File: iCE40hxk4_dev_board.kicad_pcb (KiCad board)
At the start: 4 copper layers, 70 x 152 mm, 336 parts, among them J201 CONN_01X02, J202 USB_OTG, J401 CONN_01X20, J701 CONN_01X01, J702 CONN_01X01, U1001 ADC1175, U1002 ADC1175, U1101 MIC7300, U1102 MIC7300, U1103 MCP4716, U1104 MCP4716, U1105 MIC7300, U1106 MIC7300, U201 MIC2005A-2YM5, U203 93LCxxB_sot-23-6, U204 MIC5355/6-xYMME, U205 FT2232H, U301 iCE40-HX4K-TQ144, U302 25LC_EEPROM, U501 AS4C1M16S, U701 CPC1017N, U702 CPC1017N, U703 CD4051BM96, U704 CD4051BM96, U801 CD4051BM96, U802 CD4051BM96, U803 CLC4007, U901 LM2776DBVR, U902 TCR2EF13, U903 MIC5270

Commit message: Changed part number of DAC (different dir). Connected ADC_OE to GND.
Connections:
- J202 pad 4: (no net) -> Net-(J202-Pad4)
- U1001 pad 1: (no net) -> GND
- U1001 pad 16: (no net) -> Net-(U1001-Pad16)
- U1001 pad 22: (no net) -> Net-(U1001-Pad22)
- U1002 pad 1: (no net) -> GND
- U1002 pad 16: (no net) -> Net-(U1002-Pad16)
- U1002 pad 22: (no net) -> Net-(U1002-Pad22)
- U205 pad 19: (no net) -> Net-(U205-Pad19)
- U205 pad 22: (no net) -> Net-(U205-Pad22)
- U205 pad 29: (no net) -> Net-(U205-Pad29)
- U205 pad 3: (no net) -> Net-(U205-Pad3)
- U205 pad 30: (no net) -> Net-(U205-Pad30)
- U205 pad 32: (no net) -> Net-(U205-Pad32)
- U205 pad 33: (no net) -> Net-(U205-Pad33)
- U205 pad 34: (no net) -> Net-(U205-Pad34)
- U205 pad 36: (no net) -> Net-(U205-Pad36)
- U205 pad 57: (no net) -> Net-(U205-Pad57)
- U205 pad 58: (no net) -> Net-(U205-Pad58)
- U205 pad 59: (no net) -> Net-(U205-Pad59)
- U205 pad 60: (no net) -> Net-(U205-Pad60)
- U301 pad 109: (no net) -> Net-(U301-Pad109)
- U301 pad 133: (no net) -> Net-(U301-Pad133)
- U301 pad 35: (no net) -> Net-(U301-Pad35)
- U301 pad 36: (no net) -> Net-(U301-Pad36)
- U301 pad 50: (no net) -> Net-(U301-Pad50)
- U301 pad 51: (no net) -> Net-(U301-Pad51)
- U301 pad 58: (no net) -> Net-(U301-Pad58)
- U301 pad 77: (no net) -> Net-(U301-Pad77)
- U301 pad 91: (no net) -> /RIGHT_TOP_BANKs/IOT_139
- U501 pad 33: (no net) -> Net-(U501-Pad33)
- U501 pad 37: (no net) -> Net-(U501-Pad37)
- U902 pad 4: (no net) -> Net-(U902-Pad4)
- U903 pad 1: (no net) -> Net-(U903-Pad1)
- U903 pad 3: (no net) -> Net-(U903-Pad3)
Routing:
- net /RIGHT_TOP_BANKs/IOT_139: track 0.00 -> 107.8 mm
- net (no net): track 107.8 -> 0.00 mm

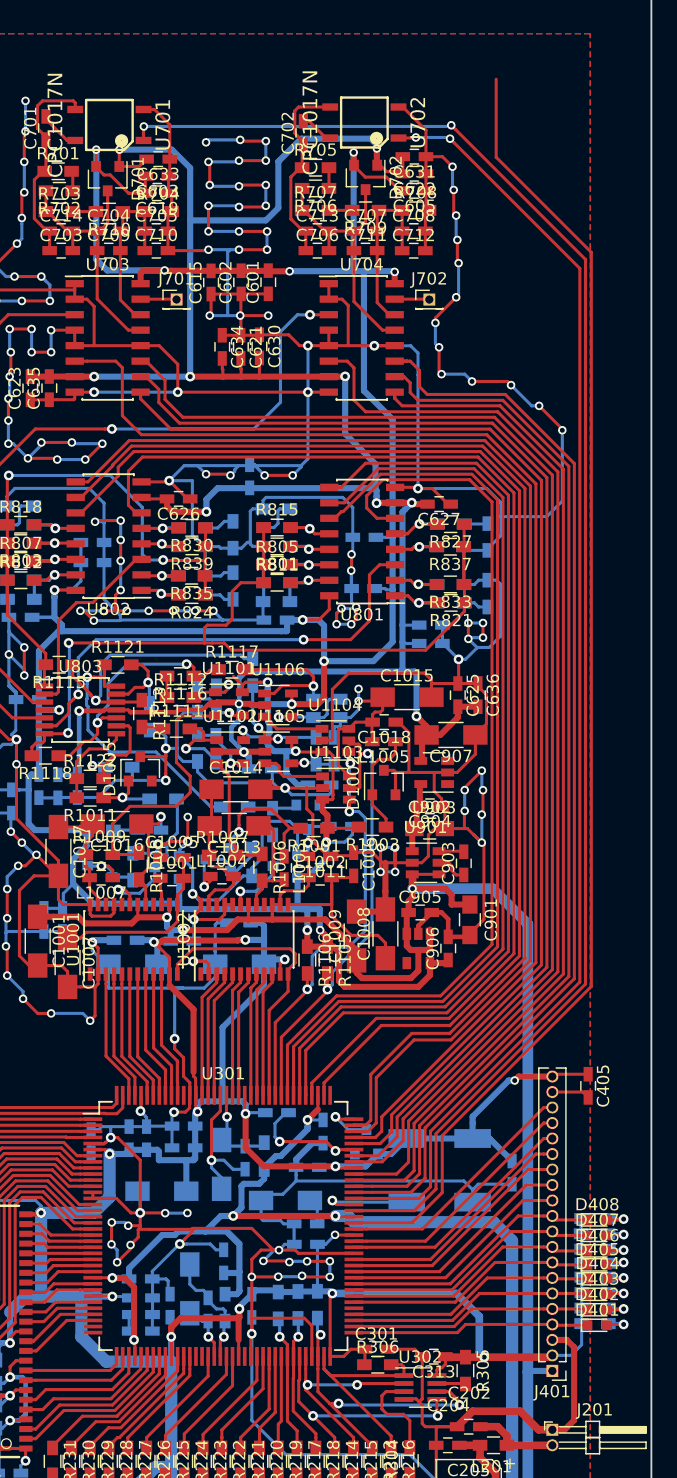
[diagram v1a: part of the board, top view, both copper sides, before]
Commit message: Added reset button. Delated unused fpga analog control connections. Added this connections to the expansion connector
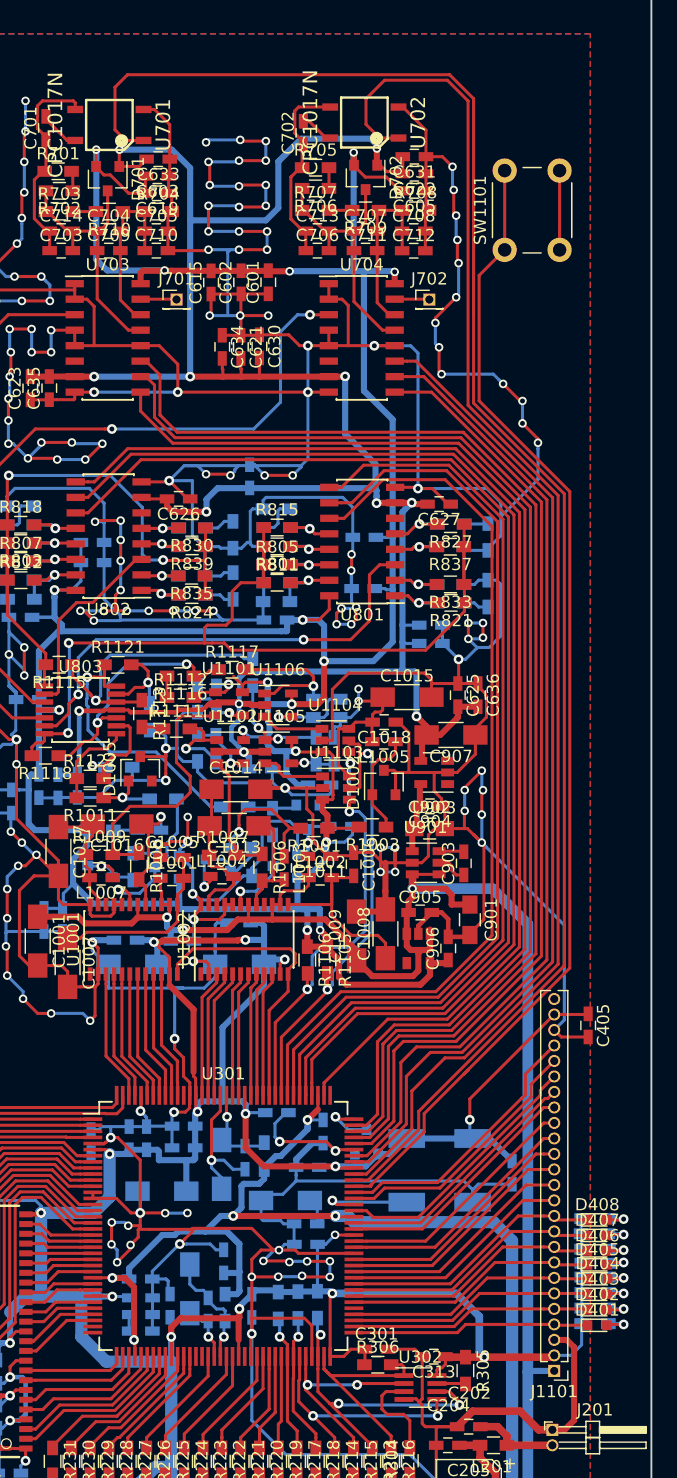
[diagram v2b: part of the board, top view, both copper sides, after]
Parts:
- removed J401: CONN_01X20, Pin_Headers:Pin_Header_Straight_1x20_Pitch1.27mm
- added J1101: CONN_01X25, Pin_Headers:Pin_Header_Straight_1x25_Pitch1.27mm, F.Cu at (146.0, 153.3)
- added SW1101: SW_Push, Buttons_Switches_THT:SW_PUSH_6mm_h4.3mm, F.Cu at (141.9, 61.4)
- moved C405 4.95 mm to (148.7, 125.0)
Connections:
- U301 pad 101: /Analog front end/CHA_ATT_SEL_0 -> /Analog front end/CHB_ATT_SEL_0
- U301 pad 102: /Analog front end/CHA_ATT_SEL_1 -> /Analog front end/CHB_ATT_SEL_1
- U301 pad 104: /Analog front end/CHA_ATT_SEL_2 -> /Analog front end/CHB_ATT_SEL_2
- U301 pad 105: /Analog front end/CHA_ATT_EN -> /Analog front end/CHA_ATT_SEL_0
- U301 pad 106: /Analog front end/CHB_GAIN_SEL_2 -> /Analog front end/CHA_ATT_SEL_1
- U301 pad 107: /Analog front end/CHB_GAIN_SEL_1 -> /Analog front end/CHA_ATT_SEL_2
- U301 pad 110: /Analog front end/CHB_GAIN_SEL_0 -> /Analog front end/CHB_GAIN_SEL_2
- U301 pad 112: /Analog front end/CHB_GAIN_EN -> /Analog front end/CHB_GAIN_SEL_1
- U301 pad 113: /Analog front end/CHA_GAIN_SEL_2 -> /Analog front end/CHB_GAIN_SEL_0
- U301 pad 114: /Analog front end/CHA_GAIN_SEL_1 -> /Analog front end/CHA_GAIN_SEL_2
- U301 pad 115: /Analog front end/CHA_GAIN_SEL_0 -> /Analog front end/CHA_GAIN_SEL_1
- U301 pad 116: /Analog front end/CHA_GAIN_EN -> /Analog front end/CHA_GAIN_SEL_0
- U301 pad 91: /RIGHT_TOP_BANKs/IOT_139 -> /RIGHT_TOP_BANKs/IOR_139
- U301 pad 93: /Analog front end/CHA_DC_COUPLING -> /RIGHT_TOP_BANKs/IOR_140
- U301 pad 95: /Analog front end/CHB_DC_COUPLING -> /RIGHT_TOP_BANKs/IOR_144
- U301 pad 96: /Analog front end/CHB_ATT_SEL_0 -> /RIGHT_TOP_BANKs/IOR_146
- U301 pad 97: /Analog front end/CHB_ATT_SEL_1 -> Net-(SW1101-Pad1)
- U301 pad 98: /Analog front end/CHB_ATT_SEL_2 -> /Analog front end/CHA_DC_COUPLING
- U301 pad 99: /Analog front end/CHB_ATT_EN -> /Analog front end/CHB_DC_COUPLING
- U703 pad 6: /Analog front end/CHA_ATT_EN -> GND
- U704 pad 6: /Analog front end/CHB_ATT_EN -> GND
- U801 pad 6: /Analog front end/CHA_GAIN_EN -> GND
- U802 pad 6: /Analog front end/CHB_GAIN_EN -> GND
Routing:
- net /RIGHT_TOP_BANKs/IOT_139: track 107.8 -> 0.00 mm
- net /Analog front end/CHA_ATT_EN: track 105.1 -> 0.00 mm
- net /Analog front end/CHB_GAIN_EN: track 97.2 -> 0.00 mm
- net Net-(SW1101-Pad1): track 0.00 -> 95.9 mm
- net /Analog front end/CHB_ATT_EN: track 90.6 -> 0.00 mm
- net /Analog front end/CHA_GAIN_EN: track 75.8 -> 0.00 mm
- net /Analog front end/CHA_DC_COUPLING: track 130.7 -> 154.3 mm, vias 2 -> 0
- net /RIGHT_TOP_BANKs/IOR_146: track 0.00 -> 22.4 mm
- net /RIGHT_TOP_BANKs/IOR_140: track 0.00 -> 21.9 mm
- net /RIGHT_TOP_BANKs/IOR_144: track 0.00 -> 21.7 mm
- net GND: track 1408.9 -> 1429.8 mm
- net /RIGHT_TOP_BANKs/IOR_139: track 0.00 -> 20.9 mm
- net /Analog front end/CHB_ATT_SEL_0: track 89.8 -> 81.0 mm
- net /Analog front end/CHB_DC_COUPLING: track 106.3 -> 114.4 mm, vias 2 -> 0
- net /Analog front end/CHB_ATT_SEL_1: track 87.1 -> 79.7 mm
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
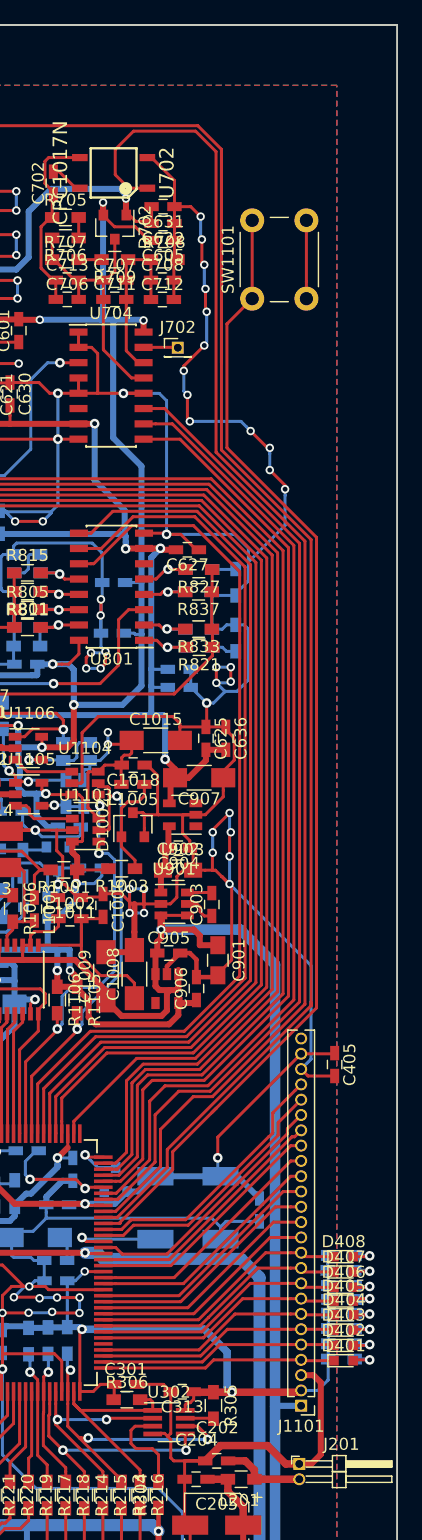
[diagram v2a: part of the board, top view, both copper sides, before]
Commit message: Added square wave output.
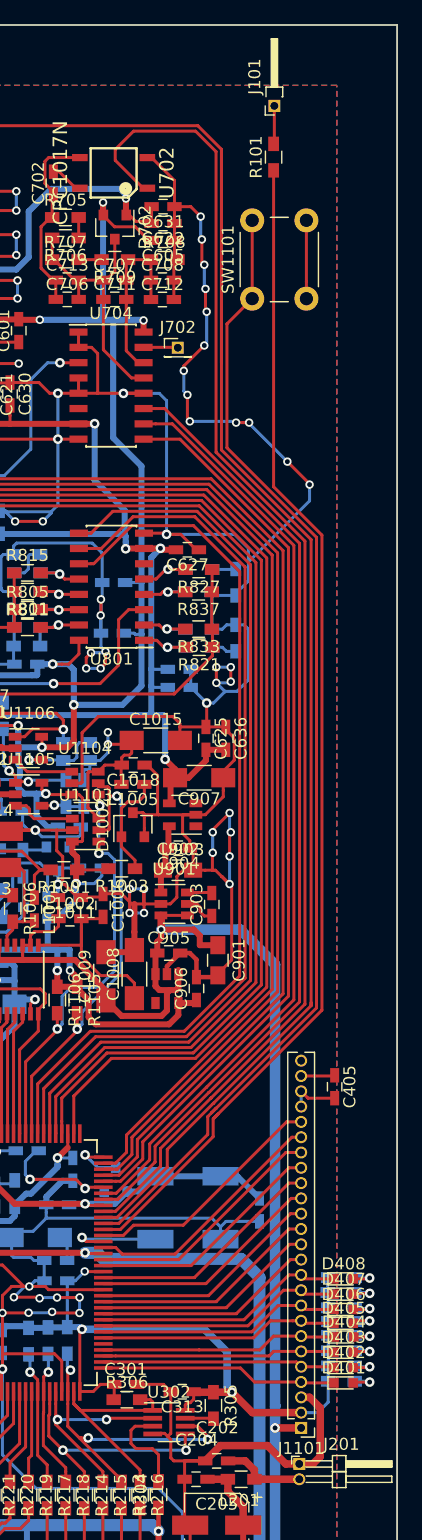
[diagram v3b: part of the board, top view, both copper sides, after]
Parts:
- added J101: CONN_01X01, Pin_Headers:Pin_Header_Angled_1x01_Pitch1.27mm, F.Cu at (143.7, 45.4)
- added R101: 10k, Resistors_SMD:R_0603_HandSoldering, F.Cu at (143.7, 49.7)
- moved D407 1.84 mm to (149.5, 144.1)
- moved R401 1.84 mm to (149.3, 151.3)
- moved C405 1.84 mm to (148.7, 126.8)
- moved D401 1.84 mm to (149.5, 151.4)
- moved D402 1.84 mm to (149.5, 150.2)
- moved D403 1.84 mm to (149.5, 148.9)
- moved D404 1.84 mm to (149.5, 147.6)
- moved D405 1.84 mm to (149.5, 146.5)
- moved D406 1.84 mm to (149.5, 145.3)
- moved D408 1.84 mm to (149.5, 142.8)
- moved J1101 1.84 mm to (146.0, 155.2)
- moved R402 1.84 mm to (149.3, 150.0)
- moved R403 1.84 mm to (149.3, 148.8)
- moved R404 1.84 mm to (149.3, 147.5)
- moved R405 1.84 mm to (149.3, 146.3)
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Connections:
- J1101 pad 22: /RIGHT_TOP_BANKs/IOR_146 -> GND
- U301 pad 96: /RIGHT_TOP_BANKs/IOR_146 -> /RIGHT_TOP_BANKs/IOT_146
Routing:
- net /RIGHT_TOP_BANKs/IOT_146: track 0.00 -> 98.3 mm
- net /RIGHT_TOP_BANKs/IOR_146: track 22.4 -> 0.00 mm
- net GND: track 1429.8 -> 1412.3 mm
- net +3V3: track 499.3 -> 487.3 mm, vias 29 -> 28
- net Net-(J101-Pad1): track 0.00 -> 3.18 mm
- net /Analog front end/CHA_ATT_SEL_2: track 95.9 -> 93.3 mm
- net /Analog front end/CHA_ATT_SEL_1: track 98.4 -> 95.8 mm
- net /Analog front end/CHA_ATT_SEL_0: track 100.6 -> 98.0 mm
- net /Analog front end/CHB_ATT_SEL_2: track 78.1 -> 75.5 mm
- net /Analog front end/CHB_ATT_SEL_1: track 79.7 -> 77.6 mm
- net /Analog front end/CHB_DC_COUPLING: track 114.4 -> 112.8 mm
- net /Analog front end/CHB_ATT_SEL_0: track 81.0 -> 79.5 mm
- net /RIGHT_TOP_BANKs/IOR_144: track 21.7 -> 20.3 mm
- net /Analog front end/CHB_GAIN_SEL_2: track 96.9 -> 98.2 mm
- net /RIGHT_TOP_BANKs/IOR_140: track 21.9 -> 20.9 mm
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
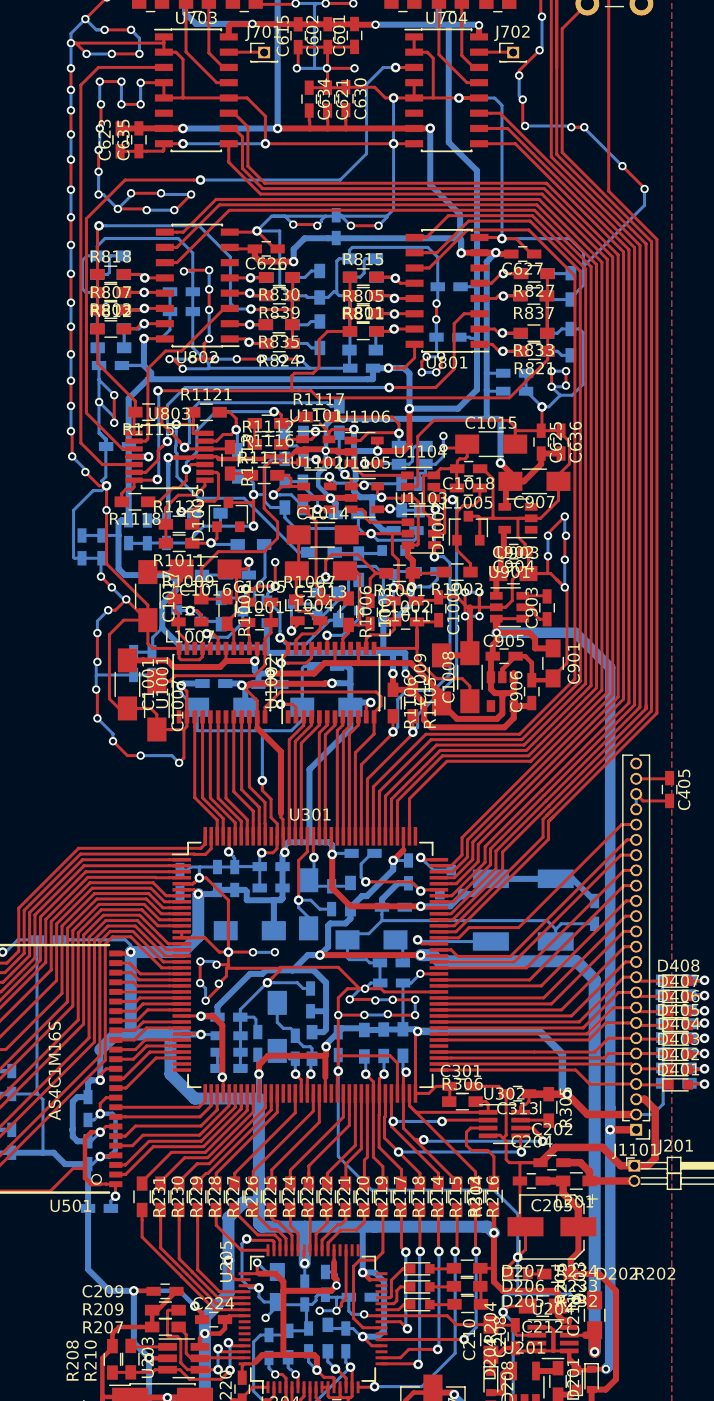
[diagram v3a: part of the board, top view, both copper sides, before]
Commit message: Moved some capacitors
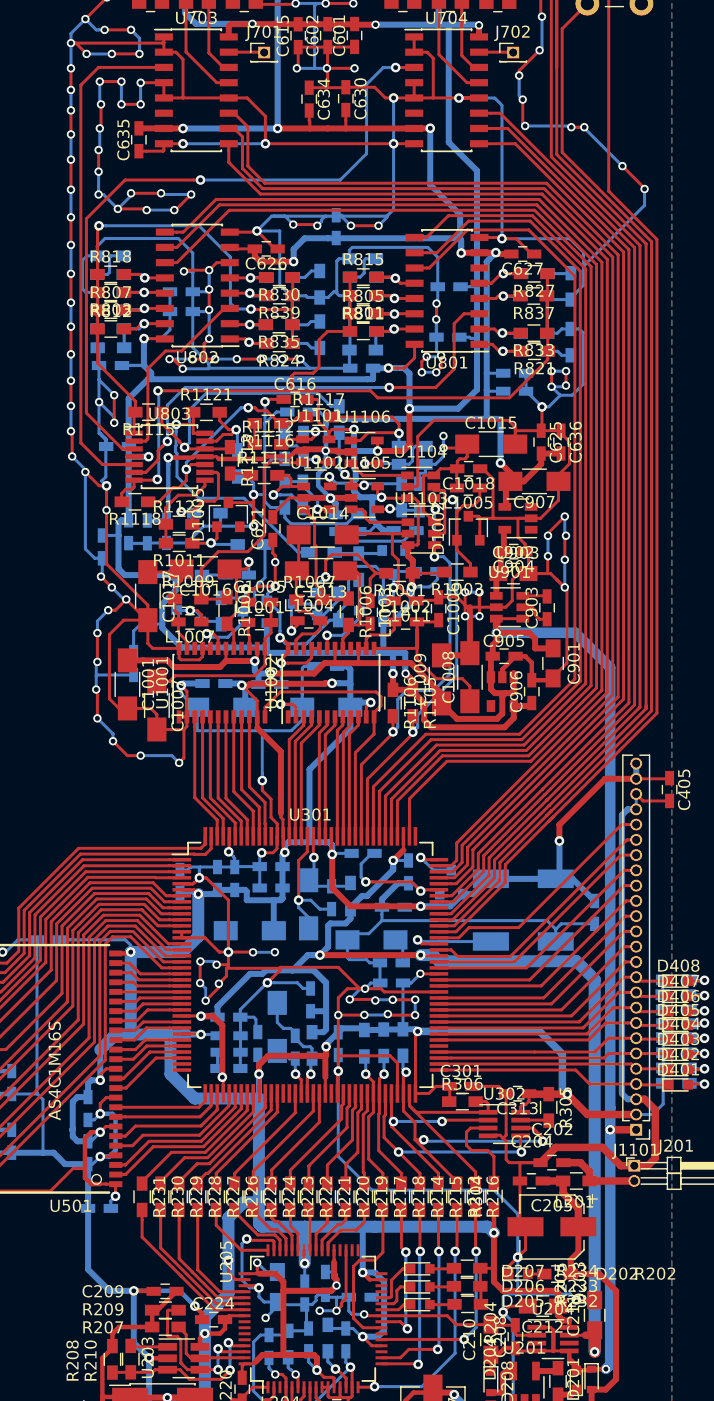
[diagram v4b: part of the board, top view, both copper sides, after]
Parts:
- C616: moved to F.Cu
- C623: moved to B.Cu
- moved C621 36.0 mm to (115.7, 105.1), turned to 90 degrees
- moved C623 27.1 mm to (117.9, 95.4), turned to 0 degrees
- moved C616 25.0 mm to (117.6, 94.4), turned to 0 degrees
- moved C608 20.5 mm to (122.0, 105.4), turned to 0 degrees
- moved C609 1.68 mm to (101.5, 106.7)
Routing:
- net GND: track 1412.3 -> 1450.0 mm
- net +3V3: track 487.3 -> 502.7 mm, vias 28 -> 29
- net /Analog front end/+3V3_A: track 303.1 -> 306.7 mm
- net /Analog front end/-3V0: track 205.1 -> 208.0 mm
- net +5V: track 157.3 -> 159.1 mm
- net /Analog front end/CHA_VREF_CENT: track 21.9 -> 20.2 mm
- net /Analog front end/PGA/CHA_G1: track 4.72 -> 6.23 mm
- net Net-(R1116-Pad1): track 20.9 -> 19.7 mm
- net Net-(R1113-Pad1): track 23.6 -> 24.4 mm
